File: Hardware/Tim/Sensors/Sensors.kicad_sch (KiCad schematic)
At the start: 13 parts, among them J1 Conn_01x02_Socket, J2 Conn_01x05_Socket, J3 Conn_01x04_Socket, U6 ICM-20948, U6 MS5607-02BA

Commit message: Reduntant board has all the stuff?
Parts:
- added J4: Conn_01x04_Socket, symbol Connector:Conn_01x04_Socket
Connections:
- net +3V3: now also J4.1 (Pin_1)
- net GND: now also J4.2 (Pin_2)
- net Ch.A renamed Ch.1A
- net Ch.B renamed Ch.1B
- new net Ch.2A: J4.3 (Pin_3)
- new net Ch.2B: J4.4 (Pin_4)
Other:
- note added: "Motor Encoder"
- note added: "String Encoder voltage maybe wrong"
- note removed: "This is a different sensor then speced"
- moved on the sheet: J3
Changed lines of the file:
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@@
     (stroke (width 0.254) (type dash))
   )
-  (wire (pts (xy 43.18 81.28) (xy 44.45 81.28))
+  (wire (pts (xy 43.18 74.93) (xy 44.45 74.93))
     (stroke (width 0) (type default))
   )
@@
     (stroke (width 0) (type default))
   )
+  (wire (pts (xy 35.56 102.87) (xy 35.56 101.6))
+    (stroke (width 0) (type default))
+  )
   (wire (pts (xy 191.77 88.9) (xy 191.77 90.17))
     (stroke (width 0) (type default))
   )
+  (wire (pts (xy 35.56 101.6) (xy 44.45 101.6))
+    (stroke (width 0) (type default))
+  )
   (wire (pts (xy 194.31 83.82) (xy 194.31 82.55))
     (stroke (width 0) (type default))
@@
     (stroke (width 0) (type default))
   )
-  (wire (pts (xy 35.56 85.09) (xy 35.56 83.82))
+  (wire (pts (xy 35.56 78.74) (xy 35.56 77.47))
     (stroke (width 0) (type default))
   )
@@
     (stroke (width 0) (type default))
   )
+  (wire (pts (xy 43.18 97.79) (xy 43.18 99.06))
+    (stroke (width 0) (type default))
+  )
   (wire (pts (xy 69.85 86.36) (xy 62.23 86.36))
     (stroke (width 0) (type default))
   )
-  (wire (pts (xy 35.56 83.82) (xy 44.45 83.82))
+  (wire (pts (xy 35.56 77.47) (xy 44.45 77.47))
     (stroke (width 0) (type default))
   )
@@
     (stroke (width 0) (type default))
   )
-  (wire (pts (xy 43.18 80.01) (xy 43.18 81.28))
+  (wire (pts (xy 43.18 73.66) (xy 43.18 74.93))
     (stroke (width 0) (type default))
   )
@@
   )
   (wire (pts (xy 142.24 95.25) (xy 142.24 100.33))
+    (stroke (width 0) (type default))
+  )
+  (wire (pts (xy 43.18 99.06) (xy 44.45 99.06))
     (stroke (width 0) (type default))
   )
@@
     (effects (font (size 2.54 2.54) (thickness 0.508) bold) (justify left bottom))
   )
-  (text "This is a different sensor then speced" (at 127 60.96 0)
+  (text "String Encoder\nvoltage maybe wrong" (at 35.56 68.58 0)
     (effects (font (size 1.27 1.27)) (justify left bottom))
   )
@@
     (effects (font (size 0.8 0.8)) (justify left bottom))
   )
+  (text "Motor Encoder" (at 36.83 92.71 0)
+    (effects (font (size 1.27 1.27)) (justify left bottom))
+  )
   (hierarchical_label "SCL" (shape input) (at 69.85 88.9 180) (fields_autoplaced)
     (effects (font (size 1.27 1.27)) (justify right))
@@
     (effects (font (size 1.27 1.27)) (justify right))
   )
+  (hierarchical_label "Ch.2B" (shape input) (at 44.45 106.68 180) (fields_autoplaced)
+    (effects (font (size 1.27 1.27)) (justify right))
+  )
   (hierarchical_label "SDA" (shape input) (at 190.5 90.17 180) (fields_autoplaced)
     (effects (font (size 1.27 1.27)) (justify right))
   )
-  (hierarchical_label "Ch.B" (shape input) (at 44.45 88.9 180) (fields_autoplaced)
+  (hierarchical_label "Ch.1B" (shape input) (at 44.45 82.55 180) (fields_autoplaced)
     (effects (font (size 1.27 1.27)) (justify right))
   )
@@
     (effects (font (size 1.27 1.27)) (justify right))
   )
+  (hierarchical_label "Ch.2A" (shape input) (at 44.45 104.14 180) (fields_autoplaced)
+    (effects (font (size 1.27 1.27)) (justify right))
+  )
   (hierarchical_label "LS1" (shape input) (at 93.98 85.09 180) (fields_autoplaced)
     (effects (font (size 1.27 1.27)) (justify right))
@@
     (effects (font (size 1.27 1.27)) (justify right))
   )
-  (hierarchical_label "Ch.A" (shape input) (at 44.45 86.36 180) (fields_autoplaced)
+  (hierarchical_label "Ch.1A" (shape input) (at 44.45 80.01 180) (fields_autoplaced)
     (effects (font (size 1.27 1.27)) (justify right))
   )
@@
     )
   )
-  (symbol (lib_id "Connector:Conn_01x04_Socket") (at 49.53 83.82 0) (unit 1)
-    (in_bom yes) (on_board yes) (dnp no)
-    (property "Reference" "J3" (at 50.8 83.82 0)
-      (effects (font (size 1.27 1.27)) (justify left))
-    )
-    (property "Value" "Conn_01x04_Socket" (at 36.83 91.44 0)
-      (effects (font (size 1.27 1.27)) (justify left))
-    )
-    (property "Footprint" "" (at 49.53 83.82 0)
-      (effects (font (size 1.27 1.27)) hide)
-    )
-    (property "Datasheet" "~" (at 49.53 83.82 0)
+  (symbol (lib_id "Connector:Conn_01x04_Socket") (at 49.53 77.47 0) (unit 1)
+    (in_bom yes) (on_board yes) (dnp no)
+    (property "Reference" "J3" (at 50.8 77.47 0)
+      (effects (font (size 1.27 1.27)) (justify left))
+    )
+    (property "Value" "Conn_01x04_Socket" (at 36.83 85.09 0)
+      (effects (font (size 1.27 1.27)) (justify left))
+    )
+    (property "Footprint" "" (at 49.53 77.47 0)
+      (effects (font (size 1.27 1.27)) hide)
+    )
+    (property "Datasheet" "~" (at 49.53 77.47 0)
       (effects (font (size 1.27 1.27)) hide)
     )
@@
     )
   )
+  (symbol (lib_id "Connector:Conn_01x04_Socket") (at 49.53 101.6 0) (unit 1)
+    (in_bom yes) (on_board yes) (dnp no)
+    (property "Reference" "J4" (at 50.8 101.6 0)
+      (effects (font (size 1.27 1.27)) (justify left))
+    )
+    (property "Value" "Conn_01x04_Socket" (at 36.83 109.22 0)
+      (effects (font (size 1.27 1.27)) (justify left))
+    )
+    (property "Footprint" "" (at 49.53 101.6 0)
+      (effects (font (size 1.27 1.27)) hide)
+    )
+    (property "Datasheet" "~" (at 49.53 101.6 0)
+      (effects (font (size 1.27 1.27)) hide)
+    )
+    (pin "1")
+    (pin "2")
+    (pin "3")
+    (pin "4")
+    (instances
+      (project "Sensors"
+        (path "/3b75f11f-e06f-4dd0-b43d-98fd40ec2e9f"
+          (reference "J4") (unit 1)
+        )
+      )
+    )
+  )
   (symbol (lib_name "GND_3") (lib_id "power:GND") (at 203.2 82.55 0) (unit 1)
     (in_bom yes) (on_board yes) (dnp no)
@@
     )
   )
-  (symbol (lib_id "power:+3V3") (at 43.18 80.01 0) (unit 1)
-    (in_bom yes) (on_board yes) (dnp no)
-    (property "Reference" "#PWR029" (at 43.18 83.82 0)
-      (effects (font (size 1.27 1.27)) hide)
-    )
-    (property "Value" "+3V3" (at 43.18 76.2 0)
-      (effects (font (size 1.27 1.27)))
-    )
-    (property "Footprint" "" (at 43.18 80.01 0)
-      (effects (font (size 1.27 1.27)) hide)
-    )
-    (property "Datasheet" "" (at 43.18 80.01 0)
+  (symbol (lib_name "GND_5") (lib_id "power:GND") (at 35.56 102.87 0) (unit 1)
+    (in_bom yes) (on_board yes) (dnp no)
+    (property "Reference" "#PWR013" (at 35.56 109.22 0)
+      (effects (font (size 1.27 1.27)) hide)
+    )
+    (property "Value" "GND" (at 35.56 106.68 0)
+      (effects (font (size 1.27 1.27)))
+    )
+    (property "Footprint" "" (at 35.56 102.87 0)
+      (effects (font (size 1.27 1.27)) hide)
+    )
+    (property "Datasheet" "" (at 35.56 102.87 0)
+      (effects (font (size 1.27 1.27)) hide)
+    )
+    (pin "1")
+    (instances
+      (project "Sensors"
+        (path "/3b75f11f-e06f-4dd0-b43d-98fd40ec2e9f"
+          (reference "#PWR013") (unit 1)
+        )
+      )
+    )
+  )
+  (symbol (lib_id "power:+3V3") (at 43.18 73.66 0) (unit 1)
+    (in_bom yes) (on_board yes) (dnp no)
+    (property "Reference" "#PWR029" (at 43.18 77.47 0)
+      (effects (font (size 1.27 1.27)) hide)
+    )
+    (property "Value" "+3V3" (at 43.18 69.85 0)
+      (effects (font (size 1.27 1.27)))
+    )
+    (property "Footprint" "" (at 43.18 73.66 0)
+      (effects (font (size 1.27 1.27)) hide)
+    )
+    (property "Datasheet" "" (at 43.18 73.66 0)
       (effects (font (size 1.27 1.27)) hide)
     )
@@
     )
   )
+  (symbol (lib_id "power:+3V3") (at 43.18 97.79 0) (unit 1)
+    (in_bom yes) (on_board yes) (dnp no)
+    (property "Reference" "#PWR029" (at 43.18 101.6 0)
+      (effects (font (size 1.27 1.27)) hide)
+    )
+    (property "Value" "+3V3" (at 43.18 93.98 0)
+      (effects (font (size 1.27 1.27)))
+    )
+    (property "Footprint" "" (at 43.18 97.79 0)
+      (effects (font (size 1.27 1.27)) hide)
+    )
+    (property "Datasheet" "" (at 43.18 97.79 0)
+      (effects (font (size 1.27 1.27)) hide)
+    )
+    (pin "1")
+    (instances
+      (project "T1000"
+        (path "/12aa2e34-1e28-4012-9c9f-3fbc422880b2"
+          (reference "#PWR029") (unit 1)
+        )
+      )
+      (project "Rudolph_Tracker"
+        (path "/131b2a79-e29c-42e9-9adf-d7be6c6c28ff"
+          (reference "#PWR049") (unit 1)
+        )
+      )
+      (project "Sensors"
+        (path "/3b75f11f-e06f-4dd0-b43d-98fd40ec2e9f"
+          (reference "#PWR014") (unit 1)
+        )
+      )
+      (project "SLAPS_Solar_Harvester"
+        (path "/65c91e2c-c4db-441a-a788-9bcdc306326f"
+          (reference "#PWR0122") (unit 1)
+        )
+      )
+      (project "BPP_Logger"
+        (path "/974c48bf-534e-4335-98e1-b0426c783e99"
+          (reference "#PWR036") (unit 1)
+        )
+      )
+      (project "GPS_Tracker"
+        (path "/b438986c-8622-4db9-bd4a-ee46786798d0"
+          (reference "#PWR056") (unit 1)
+        )
+      )
+    )
+  )
   (symbol (lib_id "Device:C_Small") (at 205.74 77.47 0) (unit 1)
     (in_bom yes) (on_board yes) (dnp no)
@@
     )
   )
-  (symbol (lib_name "GND_5") (lib_id "power:GND") (at 35.56 85.09 0) (unit 1)
-    (in_bom yes) (on_board yes) (dnp no)
-    (property "Reference" "#PWR012" (at 35.56 91.44 0)
-      (effects (font (size 1.27 1.27)) hide)
-    )
-    (property "Value" "GND" (at 35.56 88.9 0)
-      (effects (font (size 1.27 1.27)))
-    )
-    (property "Footprint" "" (at 35.56 85.09 0)
-      (effects (font (size 1.27 1.27)) hide)
-    )
-    (property "Datasheet" "" (at 35.56 85.09 0)
-      (effects (font (size 1.27 1.27)) hide)
-    )
+  (symbol (lib_name "GND_5") (lib_id "power:GND") (at 35.56 78.74 0) (unit 1)
+    (in_bom yes) (on_board yes) (dnp no)
+    (property "Reference" "#PWR012" (at 35.56 85.09 0)
+      (effects (font (size 1.27 1.27)) hide)
+    )
+    (property "Value" "GND" (at 35.56 82.55 0)
+      (effects (font (size 1.27 1.27)))
+    )
+    (property "Footprint" "" (at 35.56 78.74 0)
+      (effects (font (size 1.27 1.27)) hide)
+    )
+    (property "Datasheet" "" (at 35.56 78.74 0)
+      (effects (font (size 1.27 1.27)) hide)
+    )

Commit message: Added color sensors disconnected GPIO in muxing crisis
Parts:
- removed C20, C21, C22: 0.1 uF, symbol Device:C_Small
- removed R17, R18: 10k, symbol Device:R_Small
- removed U6: ICM-20948, Sensor_Motion:InvenSense_QFN-24_3x3mm_P0.4mm, symbol Sensor_Motion:ICM-20948
- added C1, C2: 100 nF, symbol Device:C
- added J5: Conn_01x04_Socket, symbol Connector:Conn_01x04_Socket
- added U1: BMI270, BMI270_BOS, symbol Extra symbols:BMI270
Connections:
- net +3V3: now also J5.1 (Pin_1)
- net GND: now also C1.2, C2.1, J5.2 (Pin_2), U1.6 (GNDIO), U1.7 (GND)
- net SCL: no longer J2.4 (Pin_4)
- net SDA renamed SDA_PT
- new net +3.3V: C1.1, C2.2, U1.5 (VDDIO), U1.8 (VDD)
- new net Ch.3A: J5.3 (Pin_3)
- new net Ch.3B: J5.4 (Pin_4)
- new net SCL_CLR: J2.4 (Pin_4)
- new net SPIO_CS_IMU: U1.12 (CSB)
- new net SPIO_MISO: U1.1 (SDO)
- new net SPIO_MOSI: U1.14 (SDX)
- new net SPIO_SCK: U1.13 (SCX)
- no-connect marks 6 -> 8
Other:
- note added: "Through bore encoder 1"
- note added: "Through bore encorder 2"
- note removed: "Address> LSB low"
- note removed: "String Encoder voltage maybe wrong"
- moved on the sheet: J2, J3, J4

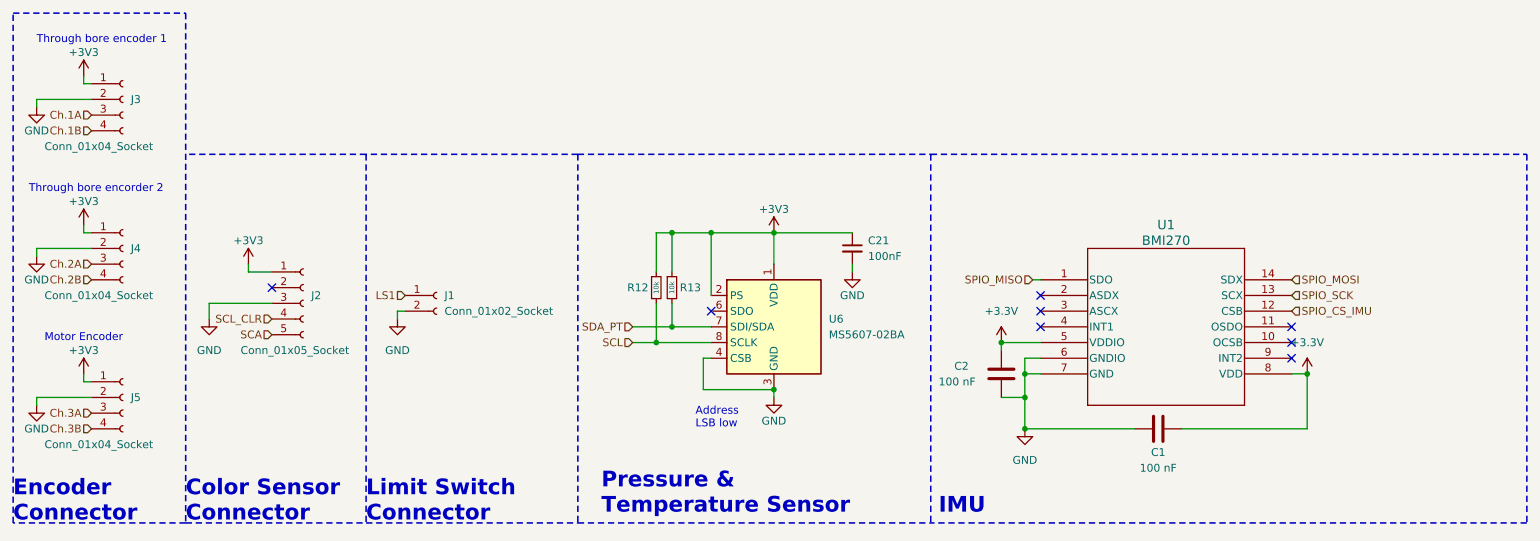
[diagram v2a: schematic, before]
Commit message: Made it all one board due to large space allowed
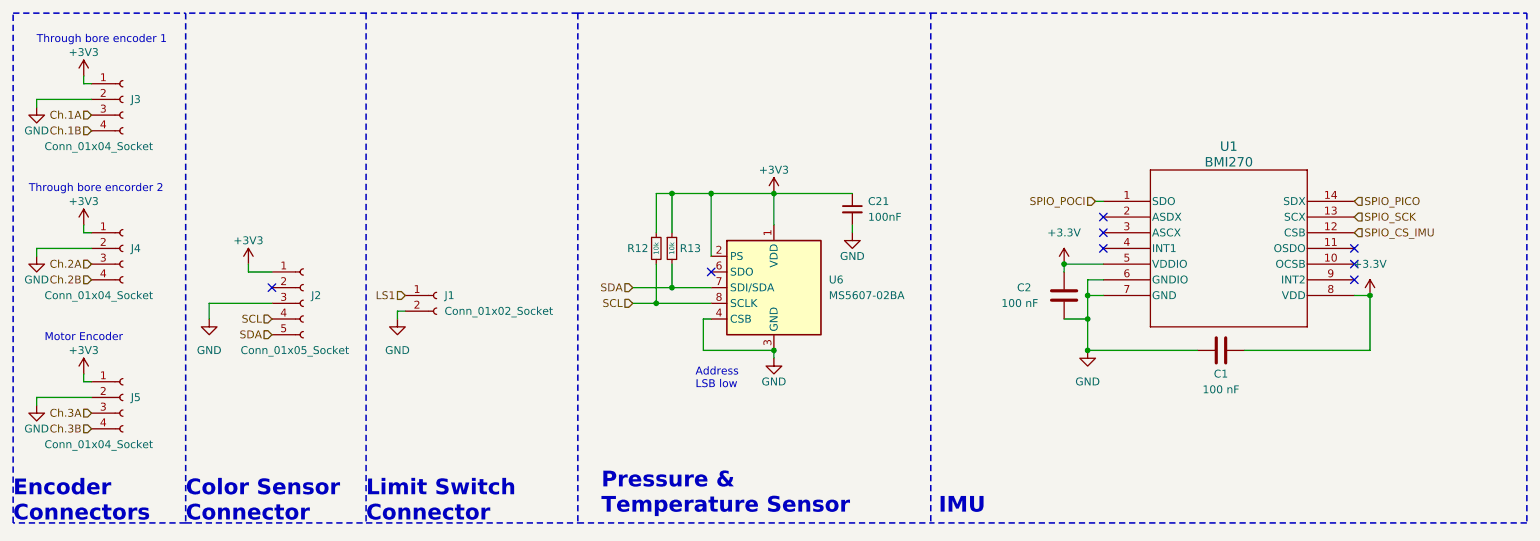
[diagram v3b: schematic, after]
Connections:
- net SCL_CLR is gone; now on net SCL: J2.4 (Pin_4)
- net SDA_PT is gone; now on net SDA: R13.2, U6.7 (SDI/SDA)
- net SCA renamed SDA
- net SPIO_MISO renamed SPIO_POCI
- net SPIO_MOSI renamed SPIO_PICO
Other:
- note added: "Encoder Connectors"
- note removed: "Encoder Connector"
- moved on the sheet: C1, C2, C21, R12, R13, U1, U6
